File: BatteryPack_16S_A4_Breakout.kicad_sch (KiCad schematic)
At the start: 0 parts

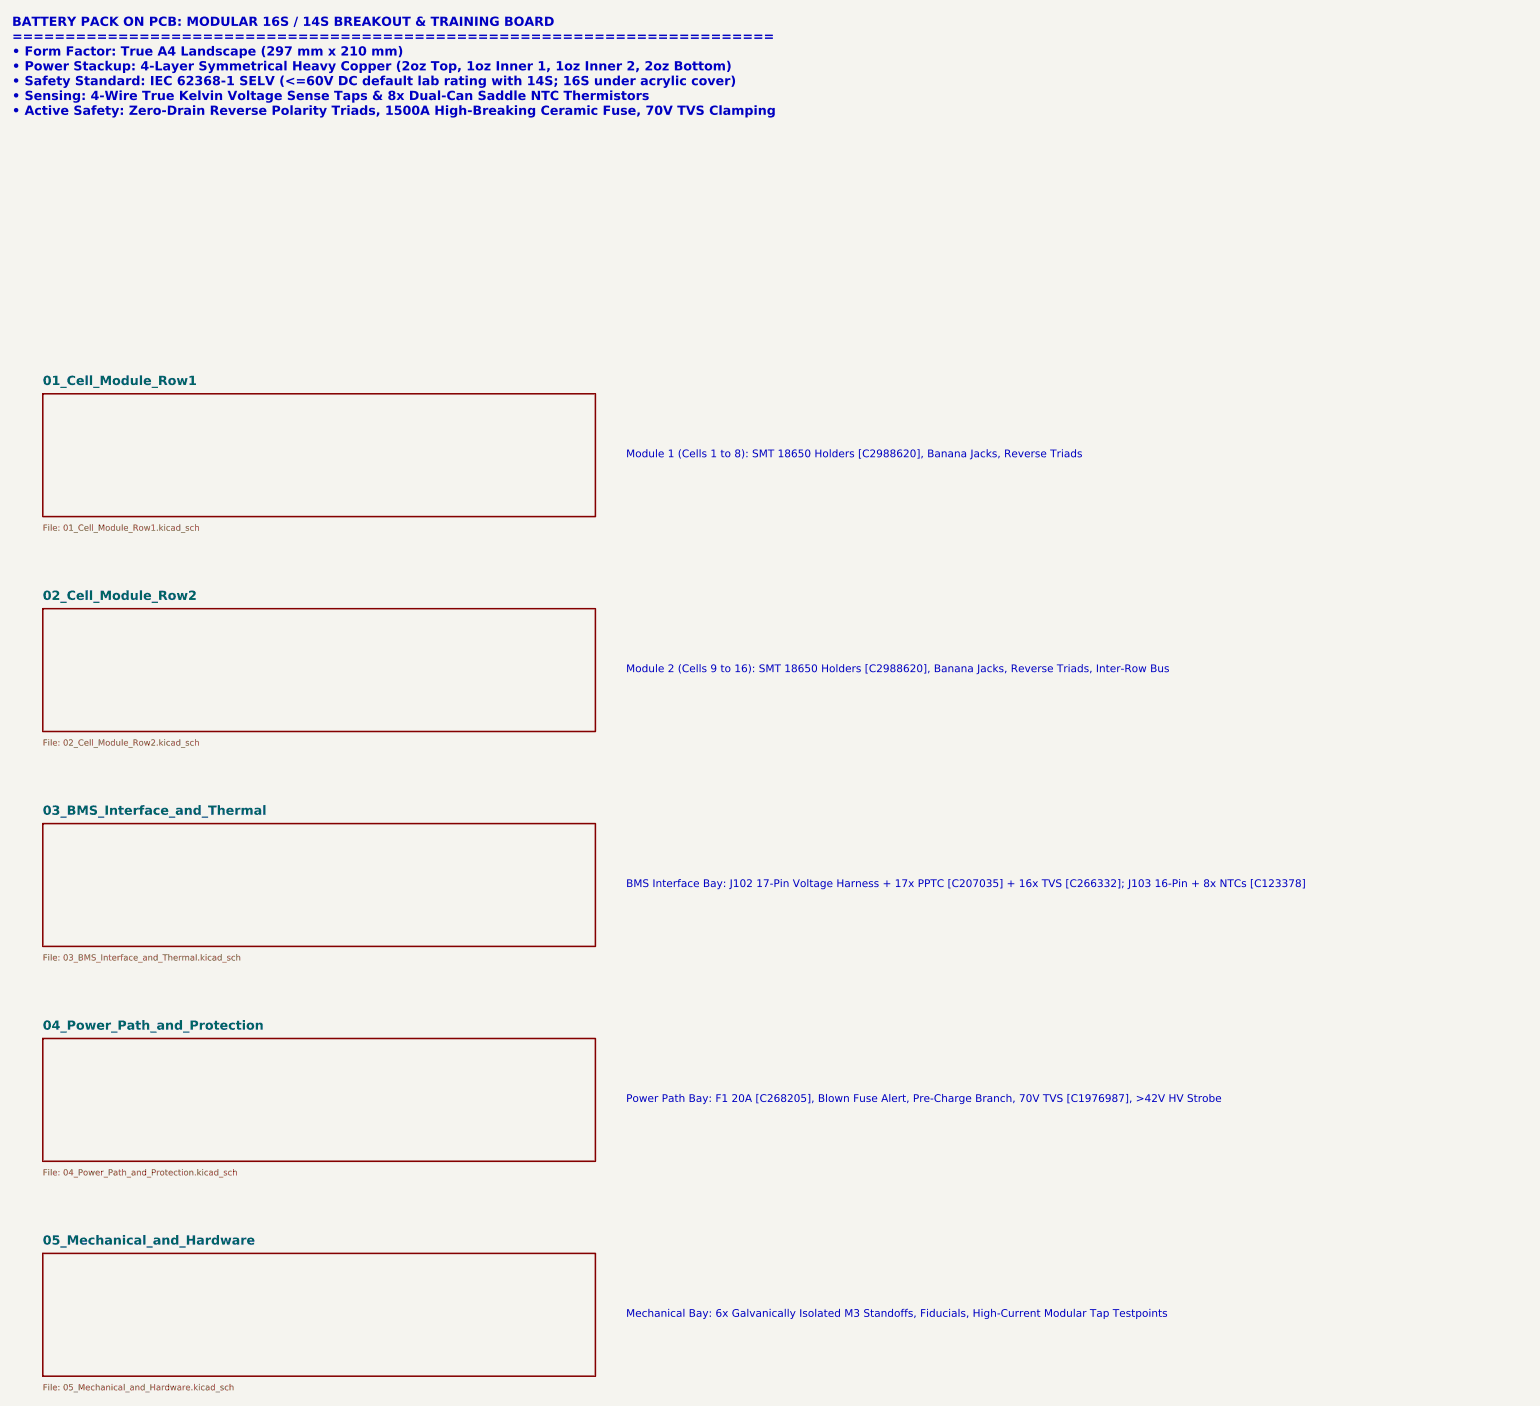
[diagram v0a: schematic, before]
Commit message: Convert pack to 14S with 7 NTC sensors, JST XH harness connectors, all-JLC BOM
- Schematic regenerated: 14 cells, 15-wire BMS sense on JST XH B15B-XH-A,
  7x 10k B3950 NTC saddles on JST XH B14B-XH-A, per-cell test loops and
  reverse-insertion indicator, power path with 5x20 fuse and M4 lugs.
- Fixes: HV zener was reversed, 4.7k/1206 HV LED resistor dissipated 0.68W
  (now 22k), 24V PPTCs on sense taps replaced with 60V MF-MSMF010-2,
  fuse-blown LED polarity corrected.
- Banana jacks (not stocked at LCSC) replaced by Keystone 5000/5001 loops.
- PCB re-laid out on the A4 (297x210) 4-layer outline: 8+6 cell columns,
  zones for cell links, sense routed on In1, NTC pairs on In2.
- ERC 0, DRC 0 (all severities), 0 unconnected, 0 schematic parity issues.
- Added Gerbers/drill zip, JLCPCB BOM + CPL, schematic PDF, renders, and the
  generator scripts in tools/.

Co-Authored-By: Claude Opus 5.5 <noreply@anthropic.com>
Claude-Session: https://claude.ai/code/session_01SDBUxKR8a94h5ECbt5NLbF
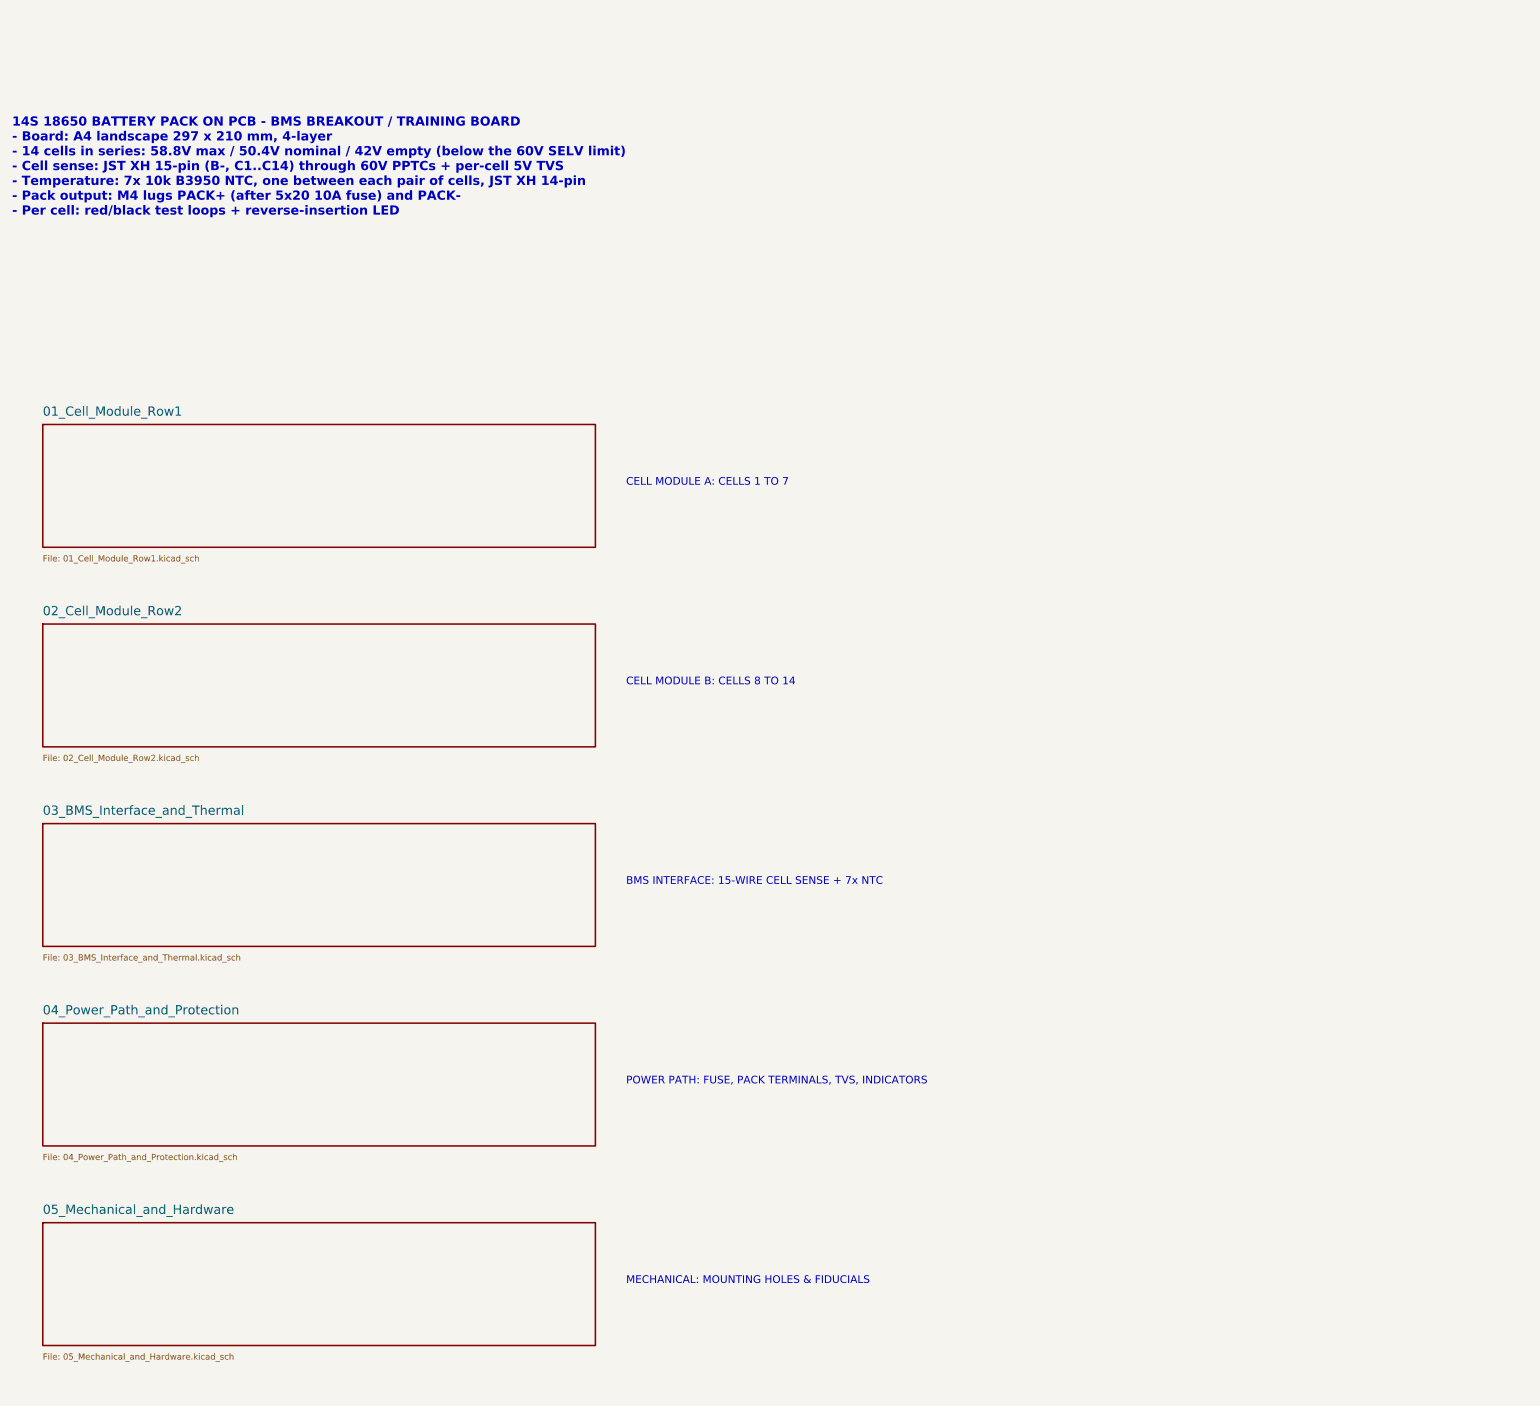
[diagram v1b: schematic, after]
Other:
- note added: "14S 18650 BATTERY PACK ON PCB - BMS BREAKOUT / TRAINING BOARD - Board: A4 landscape 297 x 210 mm, 4-layer - 14 cells in series: 58.8V max / 50.4V nominal / 42V empty (below the 60V SELV limit) - Cell sense: JST XH 15-pin (B-, C1..C14) through 60V PPTCs + per-cell 5V TVS - Temperature: 7x 10k B3950 NTC, one between each pair of cells, JST XH 14-pin - Pack output: M4 lugs PACK+ (after 5x20 10A fuse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"
- note added: "BMS INTERFACE: 15-WIRE CELL SENSE + 7x NTC"
- note added: "CELL MODULE A: CELLS 1 TO 7"
- note added: "CELL MODULE B: CELLS 8 TO 14"
- note added: "MECHANICAL: MOUNTING HOLES & FIDUCIALS"
- note added: "POWER PATH: FUSE, PACK TERMINALS, TVS, INDICATORS"
- note removed: "BATTERY PACK ON PCB: MODULAR 16S / 14S BREAKOUT & TRAINING BOARD ======================================================================== • Form Factor: True A4 Landscape (297 mm x 210 mm) • Power Stackup: 4-Layer Symmetrical Heavy Copper (2oz Top, 1oz Inner 1, 1oz Inner 2, 2oz Bottom) • Safety Standard: IEC 62368-1 SELV (<=60V DC default lab rating with 14S; 16S under acrylic cover) • Sensing: 4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"
- note removed: "BMS Interface Bay: J102 17-Pin Voltage Harness + 17x PPTC [C207035] + 16x TVS [C266332]; J103 16-Pin + 8x NTCs [C123378]"
- note removed: "Mechanical Bay: 6x Galvanically Isolated M3 Standoffs, Fiducials, High-Current Modular Tap Testpoints"
- note removed: "Module 1 (Cells 1 to 8): SMT 18650 Holders [C2988620], Banana Jacks, Reverse Triads"
- note removed: "Module 2 (Cells 9 to 16): SMT 18650 Holders [C2988620], Banana Jacks, Reverse Triads, Inter-Row Bus"
- note removed: "Power Path Bay: F1 20A [C268205], Blown Fuse Alert, Pre-Charge Branch, 70V TVS [C1976987], >42V HV Strobe"
- company: Antigravity Battery Engineering -> Battery Pack Breakout - 14S / A4
- title: BATTERY PACK ON PCB — SYSTEM ARCHITECTURE & MASTER HIERARCHY -> 14S BATTERY PACK BREAKOUT - SYSTEM ARCHITECTURE
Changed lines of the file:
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@@
 	(paper "A3")
 	(title_block
-		(title "BATTERY PACK ON PCB — SYSTEM ARCHITECTURE & MASTER HIERARCHY")
+		(title "14S BATTERY PACK BREAKOUT - SYSTEM ARCHITECTURE")
 		(date "2026-10-12")
-		(rev "Rev 1.0")
-		(company "Antigravity Battery Engineering")
-		(comment 1 "IEC 62368-1 SELV <=60V | IEC 62619 | IEEE 1625 | IPC-2152")
-		(comment 2 "Industry-Standard Modular 16S / 14S Battery Pack on PCB")
-		(comment 3 "Sheet 1 of 6")
-	)
-	(text "Mechanical Bay: 6x Galvanically Isolated M3 Standoffs, Fiducials, High-Current Modular Tap Testpoints"
-		(exclude_from_sim no)
-		(at 127 223.52 0)
-		(effects
-			(font
-				(size 1.27 1.27)
-			)
-			(justify left)
-		)
-	)
-	(text "Module 2 (Cells 9 to 16): SMT 18650 Holders [C2988620], Banana Jacks, Reverse Triads, Inter-Row Bus"
-		(exclude_from_sim no)
-		(at 127 116.84 0)
-		(effects
-			(font
-				(size 1.27 1.27)
-			)
-			(justify left)
-		)
-	)
-	(text "Power Path Bay: F1 20A [C268205], Blown Fuse Alert, Pre-Charge Branch, 70V TVS [C1976987], >42V HV Strobe"
-		(exclude_from_sim no)
-		(at 127 187.96 0)
-		(effects
-			(font
-				(size 1.27 1.27)
-			)
-			(justify left)
-		)
-	)
-	(text "Module 1 (Cells 1 to 8): SMT 18650 Holders [C2988620], Banana Jacks, Reverse Triads"
-		(exclude_from_sim no)
-		(at 127 81.28 0)
-		(effects
-			(font
-				(size 1.27 1.27)
-			)
-			(justify left)
-		)
-	)
-	(text "BATTERY PACK ON PCB: MODULAR 16S / 14S BREAKOUT & TRAINING BOARD\n========================================================================\n• Form Factor: True A4 Landscape (297 mm x 210 mm)\n• Power Stackup: 4-Layer Symmetrical Heavy Copper (2oz Top, 1oz Inner 1, 1oz Inner 2, 2oz Bottom)\n• Safety Standard: IEC 62368-1 SELV (<=60V DC default lab rating with 14S; 16S under acrylic cover)\n• Sensing: 4-Wire True Kelvin Voltage Sense Taps & 8x Dual-Can Saddle NTC Thermistors\n• Active Safety: Zero-Drain Reverse Polarity Triads, 1500A High-Breaking Ceramic Fuse, 70V TVS Clamping"
+		(rev "Rev 2.0 (14S)")
+		(company "Battery Pack Breakout - 14S / A4")
+		(comment 1 "14S Li-ion 18650 (58.8V max / 50.4V nom) | IEC 62368-1 ES2 hazard >60V not reached")
+		(comment 2 "All parts JLCPCB/LCSC sourced - LCSC field on every symbol")
+	)
+	(text "14S 18650 BATTERY PACK ON PCB - BMS BREAKOUT / TRAINING BOARD\n- Board: A4 landscape 297 x 210 mm, 4-layer\n- 14 cells in series: 58.8V max / 50.4V nominal / 42V empty (below the 60V SELV limit)\n- Cell sense: JST XH 15-pin (B-, C1..C14) through 60V PPTCs + per-cell 5V TVS\n- Temperature: 7x 10k B3950 NTC, one between each pair of cells, JST XH 14-pin\n- Pack output: M4 lugs PACK+ (after 5x20 10A fuse) and PACK-\n- Per cell: red/black test loops + reverse-insertion LED"
 		(exclude_from_sim no)
 		(at 25.4 25.4 0)
@@
 				(bold yes)
 			)
-			(justify left bottom)
-		)
-	)
-	(text "BMS Interface Bay: J102 17-Pin Voltage Harness + 17x PPTC [C207035] + 16x TVS [C266332]; J103 16-Pin + 8x NTCs [C123378]"
-		(exclude_from_sim no)
-		(at 127 152.4 0)
-		(effects
-			(font
-				(size 1.27 1.27)
-			)
-			(justify left)
-		)
-	)
-	(sheet
-		(at 30.48 71.12)
+			(justify left top)
+		)
+	)
+	(text "CELL MODULE A: CELLS 1 TO 7"
+		(exclude_from_sim no)
+		(at 127 85.09 0)
+		(effects
+			(font
+				(size 1.27 1.27)
+			)
+			(justify left top)
+		)
+	)
+	(text "CELL MODULE B: CELLS 8 TO 14"
+		(exclude_from_sim no)
+		(at 127 118.11 0)
+		(effects
+			(font
+				(size 1.27 1.27)
+			)
+			(justify left top)
+		)
+	)
+	(text "BMS INTERFACE: 15-WIRE CELL SENSE + 7x NTC"
+		(exclude_from_sim no)
+		(at 127 151.13 0)
+		(effects
+			(font
+				(size 1.27 1.27)
+			)
+			(justify left top)
+		)
+	)
+	(text "POWER PATH: FUSE, PACK TERMINALS, TVS, INDICATORS"
+		(exclude_from_sim no)
+		(at 127 184.15 0)
+		(effects
+			(font
+				(size 1.27 1.27)
+			)
+			(justify left top)
+		)
+	)
+	(text "MECHANICAL: MOUNTING HOLES & FIDUCIALS"
+		(exclude_from_sim no)
+		(at 127 217.17 0)
+		(effects
+			(font
+				(size 1.27 1.27)
+			)
+			(justify left top)
+		)
+	)
+	(sheet
+		(at 30.48 76.2)
 		(size 91.44 20.32)
 		(exclude_from_sim no)
@@
 		)
 		(property "Sheetname" "01_Cell_Module_Row1"
-			(at 30.48 69.85 0)
-			(show_name no)
-			(do_not_autoplace no)
-			(effects
-				(font
-					(size 1.524 1.524)
-					(bold yes)
+			(at 30.48 74.93 0)
+			(show_name no)
+			(do_not_autoplace no)
+			(effects
+				(font
+					(size 1.524 1.524)
 				)
 				(justify left bottom)
@@
 		)
 		(property "Sheetfile" "01_Cell_Module_Row1.kicad_sch"
-			(at 30.48 92.71 0)
-			(show_name no)
-			(do_not_autoplace no)
-			(effects
-				(font
-					(size 1.016 1.016)
-				)
-				(justify left top)
-			)
-		)
-		(instances
-			(project "BatteryPack_16S_A4_Breakout"
-				(path "/550d46ae-59f5-4417-b2d1-d9a458747a99"
+			(at 30.48 97.79 0)
+			(show_name no)
+			(do_not_autoplace no)
+			(effects
+				(font
+					(size 1.016 1.016)
+				)
+				(justify left top)
+			)
+		)
+		(instances
+			(project "BatteryPack_16S_A4_Breakout"
+				(path "/00000000-0000-0000-0000-000000000001"
 					(page "2")
 				)
@@
 	)
 	(sheet
-		(at 30.48 106.68)
+		(at 30.48 109.22)
 		(size 91.44 20.32)
 		(exclude_from_sim no)
@@
 		)
 		(property "Sheetname" "02_Cell_Module_Row2"
-			(at 30.48 105.41 0)
-			(show_name no)
-			(do_not_autoplace no)
-			(effects
-				(font
-					(size 1.524 1.524)
-					(bold yes)
+			(at 30.48 107.95 0)
+			(show_name no)
+			(do_not_autoplace no)
+			(effects
+				(font
+					(size 1.524 1.524)
 				)
 				(justify left bottom)
@@
 		)
 		(property "Sheetfile" "02_Cell_Module_Row2.kicad_sch"
-			(at 30.48 128.27 0)
-			(show_name no)
-			(do_not_autoplace no)
-			(effects
-				(font
-					(size 1.016 1.016)
-				)
-				(justify left top)
-			)
-		)
-		(instances
-			(project "BatteryPack_16S_A4_Breakout"
-				(path "/550d46ae-59f5-4417-b2d1-d9a458747a99"
+			(at 30.48 130.81 0)
+			(show_name no)
+			(do_not_autoplace no)
+			(effects
+				(font
+					(size 1.016 1.016)
+				)
+				(justify left top)
+			)
+		)
+		(instances
+			(project "BatteryPack_16S_A4_Breakout"
+				(path "/00000000-0000-0000-0000-000000000001"
 					(page "3")
 				)
@@
 				(font
 					(size 1.524 1.524)
-					(bold yes)
 				)
 				(justify left bottom)
@@
 		(instances
 			(project "BatteryPack_16S_A4_Breakout"
-				(path "/550d46ae-59f5-4417-b2d1-d9a458747a99"
+				(path "/00000000-0000-0000-0000-000000000001"
 					(page "4")
 				)
@@
 	)
 	(sheet
-		(at 30.48 177.8)
+		(at 30.48 175.26)
 		(size 91.44 20.32)
 		(exclude_from_sim no)
@@
 		)
 		(property "Sheetname" "04_Power_Path_and_Protection"
-			(at 30.48 176.53 0)
-			(show_name no)
-			(do_not_autoplace no)
-			(effects
-				(font
-					(size 1.524 1.524)
-					(bold yes)
+			(at 30.48 173.99 0)
+			(show_name no)
+			(do_not_autoplace no)
+			(effects
+				(font
+					(size 1.524 1.524)
 				)
 				(justify left bottom)
@@
 		)
 		(property "Sheetfile" "04_Power_Path_and_Protection.kicad_sch"
-			(at 30.48 199.39 0)
-			(show_name no)
-			(do_not_autoplace no)
-			(effects
-				(font
-					(size 1.016 1.016)
-				)
-				(justify left top)
-			)
-		)
-		(instances
-			(project "BatteryPack_16S_A4_Breakout"
-				(path "/550d46ae-59f5-4417-b2d1-d9a458747a99"
+			(at 30.48 196.85 0)
+			(show_name no)
+			(do_not_autoplace no)
+			(effects
+				(font
+					(size 1.016 1.016)
+				)
+				(justify left top)
+			)
+		)
+		(instances
+			(project "BatteryPack_16S_A4_Breakout"
+				(path "/00000000-0000-0000-0000-000000000001"
 					(page "5")
 				)
@@
 	)
 	(sheet
-		(at 30.48 213.36)
+		(at 30.48 208.28)
 		(size 91.44 20.32)
 		(exclude_from_sim no)
@@
 		)
 		(property "Sheetname" "05_Mechanical_and_Hardware"
-			(at 30.48 212.09 0)
-			(show_name no)
-			(do_not_autoplace no)
-			(effects
-				(font
-					(size 1.524 1.524)
-					(bold yes)
+			(at 30.48 207.01 0)
+			(show_name no)
+			(do_not_autoplace no)
+			(effects
+				(font
+					(size 1.524 1.524)
 				)
 				(justify left bottom)
@@
 		)
 		(property "Sheetfile" "05_Mechanical_and_Hardware.kicad_sch"
-			(at 30.48 234.95 0)
-			(show_name no)
-			(do_not_autoplace no)
-			(effects
-				(font
-					(size 1.016 1.016)
-				)
-				(justify left top)
-			)
-		)
-		(instances
-			(project "BatteryPack_16S_A4_Breakout"
-				(path "/550d46ae-59f5-4417-b2d1-d9a458747a99"
+			(at 30.48 229.87 0)
+			(show_name no)
+			(do_not_autoplace no)
+			(effects
+				(font
+					(size 1.016 1.016)
+				)
+				(justify left top)
+			)
+		)
+		(instances
+			(project "BatteryPack_16S_A4_Breakout"
+				(path "/00000000-0000-0000-0000-000000000001"
 					(page "6")
 				)
